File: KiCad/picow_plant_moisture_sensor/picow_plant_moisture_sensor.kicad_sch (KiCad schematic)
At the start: 31 parts, among them J1 Conn_01x03, J10 Conn_01x03, J11 Conn_01x03, J12 Conn_01x03, J13 Conn_01x03, J2 Conn_01x03, J3 Conn_01x03, J4 Conn_01x03, J5 Conn_01x03, J6 Conn_01x03, J7 Conn_02x03_Odd_Even, J8 Conn_01x03, J9 Conn_01x03, SW1 SW_Push, SW2 SW_Push, SW3 SW_Push, SW4 SW_Push, U1 TLV70033_SOT23-5, U2 PicoW, U3 ADS1115IDGS, U4 ADS1115IDGS, U5 ADS1115IDGS

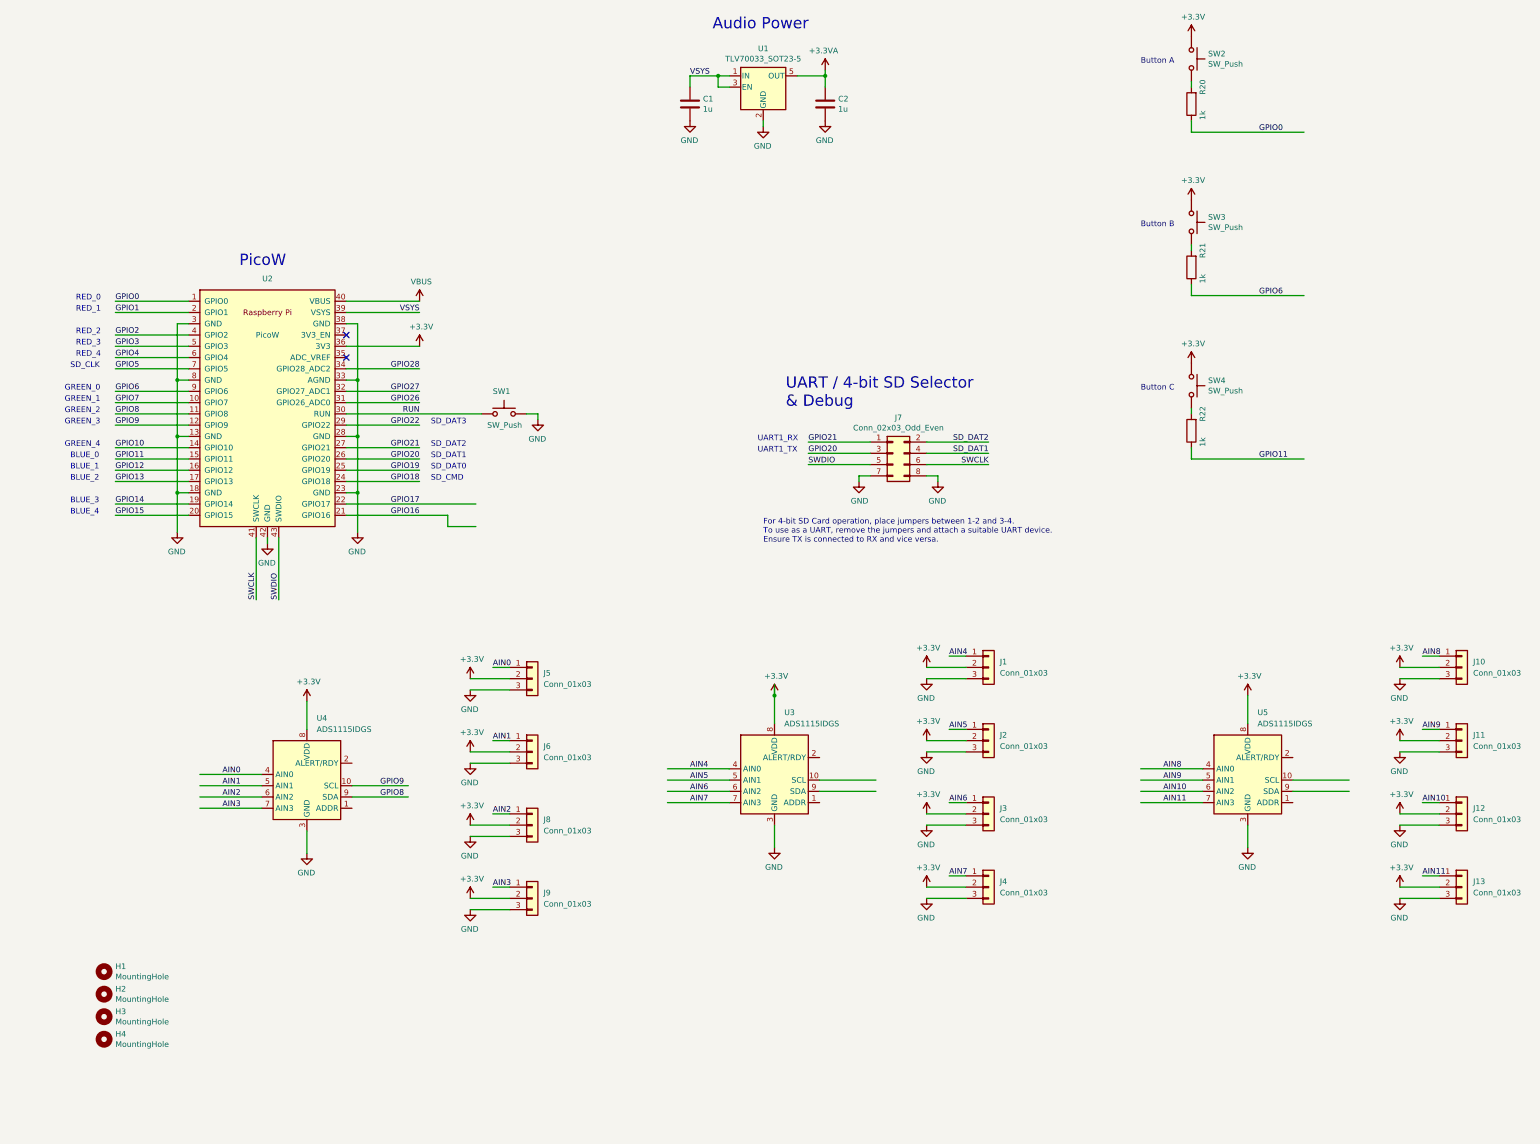
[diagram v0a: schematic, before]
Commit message: Set address on sda1115 devices
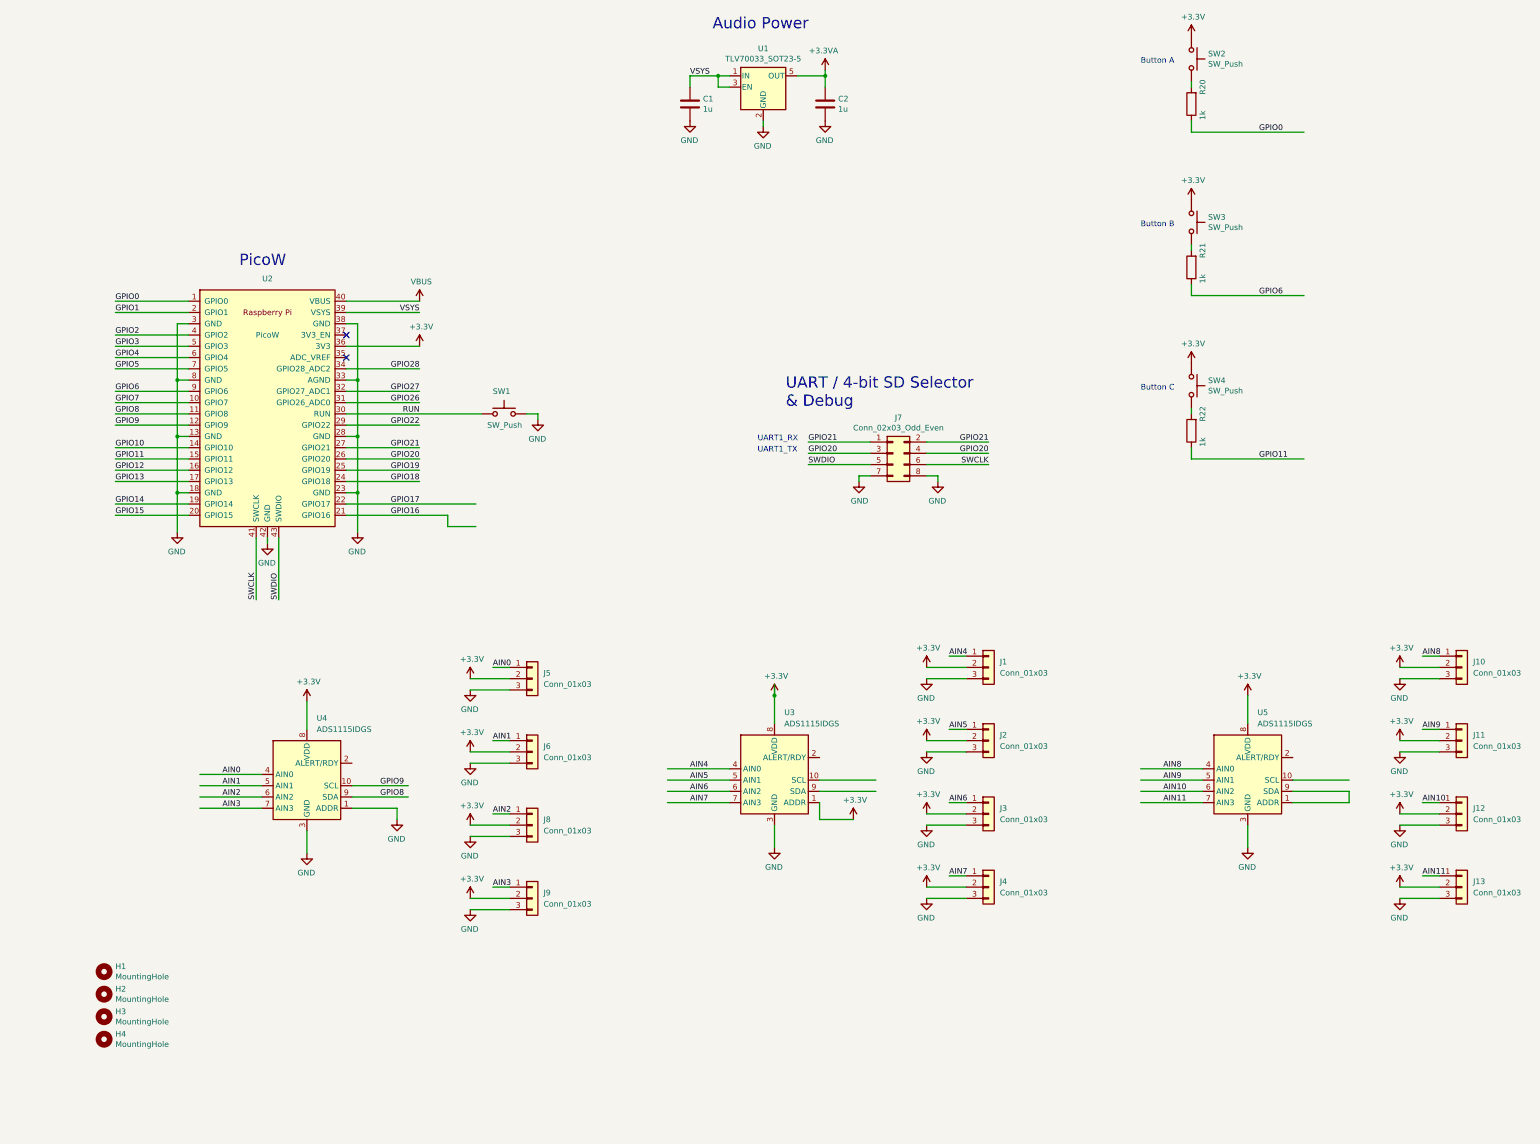
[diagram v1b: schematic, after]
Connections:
- net SD_DAT1 is gone; now on net GPIO20: J7.4 (Pin_4)
- net SD_DAT2 is gone; now on net GPIO21: J7.2 (Pin_2)
- net +3V3: now also U3.1 (ADDR)
- net GND: now also U4.1 (ADDR)
- net at U5.1 (ADDR): now also U5.9 (SDA)
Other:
- note removed: "BLUE_0"
- note removed: "BLUE_1"
- note removed: "BLUE_2"
- note removed: "BLUE_3"
- note removed: "BLUE_4"
- note removed: "For 4-bit SD Card operation, place jumpers between 1-2 and 3-4. To use as a UART, remove the jumpers and attach a suitable UART device. Ensure TX is connected to RX and vice versa."
- note removed: "GREEN_0"
- note removed: "GREEN_1"
- note removed: "GREEN_2"
- note removed: "GREEN_3"
- note removed: "GREEN_4"
- note removed: "RED_0"
- note removed: "RED_1"
- note removed: "RED_2"
- note removed: "RED_3"
- note removed: "RED_4"
- note removed: "SD_CLK"
- note removed: "SD_CMD"
- note removed: "SD_DAT0"
- note removed: "SD_DAT1"
- note removed: "SD_DAT2"
- note removed: "SD_DAT3"
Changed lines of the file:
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@@
+    (stroke (width 0) (type default))
+  )
+  (wire (pts (xy 304.8 203.2) (xy 317.5 203.2))
+    (stroke (width 0) (type default))
+  )
+  (wire (pts (xy 102.87 204.47) (xy 102.87 207.01))
     (stroke (width 0) (type default))
   )
@@
     (stroke (width 0) (type default))
   )
+  (wire (pts (xy 92.71 204.47) (xy 102.87 204.47))
+    (stroke (width 0) (type default))
+  )
   (wire (pts (xy 222.25 205.74) (xy 231.14 205.74))
     (stroke (width 0) (type default))
@@
     (stroke (width 0) (type default))
   )
+  (wire (pts (xy 198.12 207.01) (xy 205.74 207.01))
+    (stroke (width 0) (type default))
+  )
   (wire (pts (xy 91.44 125.73) (xy 107.95 125.73))
     (stroke (width 0) (type default))
@@
     (stroke (width 0) (type default))
   )
+  (wire (pts (xy 198.12 203.2) (xy 198.12 207.01))
+    (stroke (width 0) (type default))
+  )
   (wire (pts (xy 304.8 200.66) (xy 317.5 200.66))
     (stroke (width 0) (type default))
@@
     (stroke (width 0) (type default))
   )
+  (wire (pts (xy 317.5 203.2) (xy 317.5 200.66))
+    (stroke (width 0) (type default))
+  )
   (wire (pts (xy 55.88 95.25) (xy 53.34 95.25))
     (stroke (width 0) (type default))
@@
     (stroke (width 0) (type default))
   )
-  (text "GREEN_0" (at 27.94 110.49 0)
-    (effects (font (size 1.27 1.27)) (justify left bottom))
-  )
-  (text "RED_3" (at 30.48 100.33 0)
-    (effects (font (size 1.27 1.27)) (justify left bottom))
-  )
-  (text "RED_1" (at 30.48 92.71 0)
-    (effects (font (size 1.27 1.27)) (justify left bottom))
-  )
-  (text "SD_DAT2" (at 110.49 123.19 0)
-    (effects (font (size 1.27 1.27)) (justify left bottom))
-  )
   (text "Button A" (at 270.51 36.83 0)
     (effects (font (size 1.27 1.27)) (justify left bottom))
   )
-  (text "SD_CLK" (at 29.21 105.41 0)
-    (effects (font (size 1.27 1.27)) (justify left bottom))
-  )
-  (text "BLUE_4" (at 29.21 138.43 0)
-    (effects (font (size 1.27 1.27)) (justify left bottom))
-  )
-  (text "BLUE_0" (at 29.21 125.73 0)
-    (effects (font (size 1.27 1.27)) (justify left bottom))
-  )
   (text "UART1_TX " (at 184.15 124.46 0)
-    (effects (font (size 1.27 1.27)) (justify left bottom))
-  )
-  (text "SD_DAT1" (at 110.49 125.73 0)
-    (effects (font (size 1.27 1.27)) (justify left bottom))
-  )
-  (text "RED_4" (at 30.48 102.87 0)
     (effects (font (size 1.27 1.27)) (justify left bottom))
   )
@@
     (effects (font (size 2.54 2.54)) (justify left bottom))
   )
-  (text "For 4-bit SD Card operation, place jumpers between 1-2 and 3-4.\nTo use as a UART, remove the jumpers and attach a suitable UART device.\nEnsure TX is connected to RX and vice versa.\n"
-    (at 185.42 144.78 0)
-    (effects (font (size 1.27 1.27)) (justify left bottom))
-  )
   (text "UART1_RX" (at 184.15 121.92 0)
     (effects (font (size 1.27 1.27)) (justify left bottom))
@@
   )
   (text "Button C" (at 270.51 110.49 0)
-    (effects (font (size 1.27 1.27)) (justify left bottom))
-  )
-  (text "GREEN_1" (at 27.94 113.03 0)
     (effects (font (size 1.27 1.27)) (justify left bottom))
   )
@@
     (effects (font (size 2.54 2.54)) (justify left bottom))
   )
-  (text "SD_DAT0" (at 110.49 128.27 0)
-    (effects (font (size 1.27 1.27)) (justify left bottom))
-  )
-  (text "BLUE_3" (at 29.21 135.89 0)
-    (effects (font (size 1.27 1.27)) (justify left bottom))
-  )
-  (text "SD_CMD" (at 110.49 130.81 0)
-    (effects (font (size 1.27 1.27)) (justify left bottom))
-  )
-  (text "SD_DAT3" (at 110.49 118.11 0)
-    (effects (font (size 1.27 1.27)) (justify left bottom))
-  )
-  (text "GREEN_4" (at 27.94 123.19 0)
-    (effects (font (size 1.27 1.27)) (justify left bottom))
-  )
-  (text "RED_2" (at 30.48 97.79 0)
-    (effects (font (size 1.27 1.27)) (justify left bottom))
-  )
-  (text "GREEN_2" (at 27.94 115.57 0)
-    (effects (font (size 1.27 1.27)) (justify left bottom))
-  )
   (text "Audio Power" (at 173.99 29.21 0)
     (effects (font (size 2.54 2.54)) (justify left bottom))
   )
-  (text "BLUE_1" (at 29.21 128.27 0)
-    (effects (font (size 1.27 1.27)) (justify left bottom))
-  )
-  (text "GREEN_3" (at 27.94 118.11 0)
-    (effects (font (size 1.27 1.27)) (justify left bottom))
-  )
-  (text "BLUE_2" (at 29.21 130.81 0)
-    (effects (font (size 1.27 1.27)) (justify left bottom))
-  )
-  (text "RED_0" (at 30.48 90.17 0)
-    (effects (font (size 1.27 1.27)) (justify left bottom))
-  )
   (label "GPIO14" (at 39.37 135.89 0) (fields_autoplaced)
     (effects (font (size 1.27 1.27)) (justify left bottom))
@@
     (effects (font (size 1.27 1.27)) (justify left bottom))
   )
-  (label "SD_DAT1" (at 236.22 124.46 180) (fields_autoplaced)
+  (label "GPIO20" (at 236.22 124.46 180) (fields_autoplaced)
     (effects (font (size 1.27 1.27)) (justify right bottom))
   )
@@
     (effects (font (size 1.27 1.27)) (justify left bottom))
   )
-  (label "SD_DAT2" (at 236.22 121.92 180) (fields_autoplaced)
+  (label "GPIO21" (at 236.22 121.92 180) (fields_autoplaced)
     (effects (font (size 1.27 1.27)) (justify right bottom))
   )
@@
     )
   )
+  (symbol (lib_id "power:+3.3V") (at 205.74 207.01 0) (unit 1)
+    (in_bom yes) (on_board yes) (dnp no)
+    (property "Reference" "#PWR033" (at 205.74 210.82 0)
+      (effects (font (size 1.27 1.27)) hide)
+    )
+    (property "Value" "+3.3V" (at 206.121 202.6158 0)
+      (effects (font (size 1.27 1.27)))
+    )
+    (property "Footprint" "" (at 205.74 207.01 0)
+      (effects (font (size 1.27 1.27)) hide)
+    )
+    (property "Datasheet" "" (at 205.74 207.01 0)
+      (effects (font (size 1.27 1.27)) hide)
+    )
+    (pin "1")
+    (instances
+      (project "picow_plant_moisture_sensor"
+        (path "/7e7c068a-a341-4358-ab45-53bb7a793d6f"
+          (reference "#PWR033") (unit 1)
+        )
+      )
+    )
+  )
   (symbol (lib_id "power:+3.3V") (at 328.93 172.72 0) (unit 1)
     (in_bom yes) (on_board yes) (dnp no)
@@
         )
       )
+    )
+  )
+  (symbol (lib_id "power:GND") (at 102.87 207.01 0) (mirror y) (unit 1)
+    (in_bom yes) (on_board yes) (dnp no)
+    (property "Reference" "#PWR032" (at 102.87 213.36 0)
+      (effects (font (size 1.27 1.27)) hide)
+    )
+    (property "Value" "GND" (at 102.743 211.4042 0)
+      (effects (font (size 1.27 1.27)))
+    )
+    (property "Footprint" "" (at 102.87 207.01 0)
+      (effects (font (size 1.27 1.27)) hide)
+    )
+    (property "Datasheet" "" (at 102.87 207.01 0)
+      (effects (font (size 1.27 1.27)) hide)
+    )
+    (pin "1")
+    (instances
+      (project "picow_plant_moisture_sensor"
+        (path "/7e7c068a-a341-4358-ab45-53bb7a793d6f"
+          (reference "#PWR032") (unit 1)
+        )
+      )

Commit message: First version done
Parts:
- removed C1, C2: 1u, Capacitor_SMD:C_0603_1608Metric, symbol Device:C
- removed U1: TLV70033_SOT23-5, Package_TO_SOT_SMD:SOT-23-5, symbol Regulator_Linear:TLV70033_SOT23-5
- removed U3, U4, U5: ADS1115IDGS, Package_SO:TSSOP-10_3x3mm_P0.5mm, symbol Analog_ADC:ADS1115IDGS
- added J14, J15, J16: ADS1115, Connector_PinHeader_2.54mm:PinHeader_1x10_P2.54mm_Horizontal, symbol Connector_Generic:Conn_01x10
- J1, J10, J11, J12, J13, J2, J3, J4, J5, J6, J8, J9: footprint (none) -> Connector_PinHeader_2.54mm:PinHeader_1x03_P2.54mm_Horizontal
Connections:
- net +3V3: now also J14.10 (Pin_10), J15.10 (Pin_10), J15.6 (Pin_6), J16.10 (Pin_10)
- net AIN0: now also J16.4 (Pin_4)
- net AIN1: now also J16.3 (Pin_3)
- net AIN10: now also J14.2 (Pin_2)
- net AIN11: now also J14.1 (Pin_1)
- net AIN2: now also J16.2 (Pin_2)
- net AIN3: now also J16.1 (Pin_1)
- net AIN4: now also J15.4 (Pin_4)
- net AIN5: now also J15.3 (Pin_3)
- net AIN6: now also J15.2 (Pin_2)
- net AIN7: now also J15.1 (Pin_1)
- net AIN8: now also J14.4 (Pin_4)
- net AIN9: now also J14.3 (Pin_3)
- net GND: now also J14.9 (Pin_9), J15.9 (Pin_9), J16.6 (Pin_6), J16.9 (Pin_9)
- net GPIO8: now also J14.6 (Pin_6), J14.7 (Pin_7), J15.7 (Pin_7), J16.7 (Pin_7)
- net GPIO9: now also J14.8 (Pin_8), J15.8 (Pin_8), J16.8 (Pin_8)
- no-connect marks 2 -> 24
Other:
- note removed: "Audio Power"
- moved on the sheet: J1, J10, J11, J12, J13, J2, J3, J4, J5, J6, J8, J9

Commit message: V1 done
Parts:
- J1, J10, J11, J12, J13, J2, J3, J4, J5, J6, J8, J9: footprint Connector_PinHeader_2.54mm:PinHeader_1x03_P2.54mm_Horizontal -> Connector_PinHeader_2.54mm:PinHeader_1x03_P2.54mm_Vertical
- J14, J15, J16: footprint Connector_PinHeader_2.54mm:PinHeader_1x10_P2.54mm_Horizontal -> Connector_PinHeader_2.54mm:PinHeader_1x10_P2.54mm_Vertical
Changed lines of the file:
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@@
       (effects (font (size 1.27 1.27)) (justify left))
     )
-    (property "Footprint" "Connector_PinHeader_2.54mm:PinHeader_1x03_P2.54mm_Horizontal" (at 128.27 177.8 0)
+    (property "Footprint" "Connector_PinHeader_2.54mm:PinHeader_1x03_P2.54mm_Vertical" (at 128.27 177.8 0)
       (effects (font (size 1.27 1.27)) hide)
     )
@@
       (effects (font (size 1.27 1.27)) (justify left))
     )
-    (property "Footprint" "Connector_PinHeader_2.54mm:PinHeader_1x03_P2.54mm_Horizontal" (at 128.27 227.33 0)
+    (property "Footprint" "Connector_PinHeader_2.54mm:PinHeader_1x03_P2.54mm_Vertical" (at 128.27 227.33 0)
       (effects (font (size 1.27 1.27)) hide)
     )
@@
       (effects (font (size 1.27 1.27)) (justify left))
     )
-    (property "Footprint" "Connector_PinHeader_2.54mm:PinHeader_1x03_P2.54mm_Horizontal" (at 128.27 194.31 0)
+    (property "Footprint" "Connector_PinHeader_2.54mm:PinHeader_1x03_P2.54mm_Vertical" (at 128.27 194.31 0)
       (effects (font (size 1.27 1.27)) hide)
     )
@@
       (effects (font (size 1.27 1.27)) (justify left))
     )
-    (property "Footprint" "Connector_PinHeader_2.54mm:PinHeader_1x03_P2.54mm_Horizontal" (at 306.07 227.33 0)
+    (property "Footprint" "Connector_PinHeader_2.54mm:PinHeader_1x03_P2.54mm_Vertical" (at 306.07 227.33 0)
       (effects (font (size 1.27 1.27)) hide)
     )
@@
       (effects (font (size 1.27 1.27)) (justify left))
     )
-    (property "Footprint" "Connector_PinHeader_2.54mm:PinHeader_1x10_P2.54mm_Horizontal" (at 176.53 201.93 0)
+    (property "Footprint" "Connector_PinHeader_2.54mm:PinHeader_1x10_P2.54mm_Vertical" (at 176.53 201.93 0)
       (effects (font (size 1.27 1.27)) hide)
     )
@@
       (effects (font (size 1.27 1.27)) (justify left))
     )
-    (property "Footprint" "Connector_PinHeader_2.54mm:PinHeader_1x10_P2.54mm_Horizontal" (at 267.97 201.93 0)
+    (property "Footprint" "Connector_PinHeader_2.54mm:PinHeader_1x10_P2.54mm_Vertical" (at 267.97 201.93 0)
       (effects (font (size 1.27 1.27)) hide)
     )
@@
       (effects (font (size 1.27 1.27)) (justify left))
     )
-    (property "Footprint" "Connector_PinHeader_2.54mm:PinHeader_1x03_P2.54mm_Horizontal" (at 306.07 210.82 0)
+    (property "Footprint" "Connector_PinHeader_2.54mm:PinHeader_1x03_P2.54mm_Vertical" (at 306.07 210.82 0)
       (effects (font (size 1.27 1.27)) hide)
     )
@@
       (effects (font (size 1.27 1.27)) (justify left))
     )
-    (property "Footprint" "Connector_PinHeader_2.54mm:PinHeader_1x03_P2.54mm_Horizontal" (at 217.17 210.82 0)
+    (property "Footprint" "Connector_PinHeader_2.54mm:PinHeader_1x03_P2.54mm_Vertical" (at 217.17 210.82 0)
       (effects (font (size 1.27 1.27)) hide)
     )
@@
       (effects (font (size 1.27 1.27)) (justify left))
     )
-    (property "Footprint" "Connector_PinHeader_2.54mm:PinHeader_1x03_P2.54mm_Horizontal" (at 306.07 194.31 0)
+    (property "Footprint" "Connector_PinHeader_2.54mm:PinHeader_1x03_P2.54mm_Vertical" (at 306.07 194.31 0)
       (effects (font (size 1.27 1.27)) hide)
     )
@@
       (effects (font (size 1.27 1.27)) (justify left))
     )
-    (property "Footprint" "Connector_PinHeader_2.54mm:PinHeader_1x03_P2.54mm_Horizontal" (at 217.17 194.31 0)
+    (property "Footprint" "Connector_PinHeader_2.54mm:PinHeader_1x03_P2.54mm_Vertical" (at 217.17 194.31 0)
       (effects (font (size 1.27 1.27)) hide)
     )
@@
       (effects (font (size 1.27 1.27)) (justify left))
     )
-    (property "Footprint" "Connector_PinHeader_2.54mm:PinHeader_1x03_P2.54mm_Horizontal" (at 306.07 177.8 0)
+    (property "Footprint" "Connector_PinHeader_2.54mm:PinHeader_1x03_P2.54mm_Vertical" (at 306.07 177.8 0)
       (effects (font (size 1.27 1.27)) hide)
     )
@@
       (effects (font (size 1.27 1.27)) (justify left))
     )
-    (property "Footprint" "Connector_PinHeader_2.54mm:PinHeader_1x03_P2.54mm_Horizontal" (at 217.17 177.8 0)
+    (property "Footprint" "Connector_PinHeader_2.54mm:PinHeader_1x03_P2.54mm_Vertical" (at 217.17 177.8 0)
       (effects (font (size 1.27 1.27)) hide)
     )
@@
       (effects (font (size 1.27 1.27)) (justify left))
     )
-    (property "Footprint" "Connector_PinHeader_2.54mm:PinHeader_1x03_P2.54mm_Horizontal" (at 217.17 227.33 0)
+    (property "Footprint" "Connector_PinHeader_2.54mm:PinHeader_1x03_P2.54mm_Vertical" (at 217.17 227.33 0)
       (effects (font (size 1.27 1.27)) hide)
     )
@@
       (effects (font (size 1.27 1.27)) (justify left))
     )
-    (property "Footprint" "Connector_PinHeader_2.54mm:PinHeader_1x10_P2.54mm_Horizontal" (at 87.63 201.93 0)
+    (property "Footprint" "Connector_PinHeader_2.54mm:PinHeader_1x10_P2.54mm_Vertical" (at 87.63 201.93 0)
       (effects (font (size 1.27 1.27)) hide)
     )
@@
       (effects (font (size 1.27 1.27)) (justify left))
     )
-    (property "Footprint" "Connector_PinHeader_2.54mm:PinHeader_1x03_P2.54mm_Horizontal" (at 128.27 210.82 0)
-      (effects (font (size 1.27 1.27)) hide)
-    )
+    (property "Footprint" "Connector_PinHeader_2.54mm:PinHeader_1x03_P2.54mm_Vertical" (at 128.27 210.82 0)
+      (effects (font (size 1.27 1.27)) hide)
+    )
